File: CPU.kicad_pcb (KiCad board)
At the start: 4 copper layers, 364 x 203 mm, 219 parts, among them J1 Conn_02x36_Top_Bottom, P10 Conn_02x08_Counter_Clockwise, P2 Conn_02x13_Top_Bottom, P3 Conn_02x13_Top_Bottom, P4 Conn_02x08_Counter_Clockwise, P5 Conn_02x25_Counter_Clockwise, P6 Conn_02x25_Counter_Clockwise, P7 Conn_02x07_Counter_Clockwise, P8 Conn_02x08_Counter_Clockwise

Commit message: Second row completed
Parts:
- moved U_B10 0.51 mm to (339.9, 148.4)
- moved U_B9 0.51 mm to (339.9, 135.2)
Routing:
- net Net-(JP1-Pad3): track 16.0 -> 108.8 mm, vias 0 -> 1
- net /Sys.Reset: track 59.1 -> 130.5 mm
- net Net-(U_B7-Pad1): track 0.00 -> 70.3 mm, vias 0 -> 1
- net Net-(U_A15-Pad9): track 0.00 -> 60.9 mm, vias 0 -> 1
- net Address.A_{15}: track 66.0 -> 110.3 mm
- net Net-(U_B6-Pad15): track 0.00 -> 42.8 mm
- net /PTR.Q_{6}: track 96.1 -> 126.6 mm, vias 1 -> 2
- net /~{H14_OE}: track 79.8 -> 105.5 mm
- net /PTR.Q_{5}: track 173.2 -> 182.6 mm
- net /J13_12: track 44.6 -> 51.2 mm
- net Address.A_{12}: track 179.3 -> 173.6 mm
- net Address.A_{14}: track 172.5 -> 166.9 mm
- net Address.A_{13}: track 178.0 -> 174.4 mm
- net Res.D_{3}: track 147.8 -> 144.2 mm
- net /~{AddrHToSys}: track 171.4 -> 168.9 mm
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
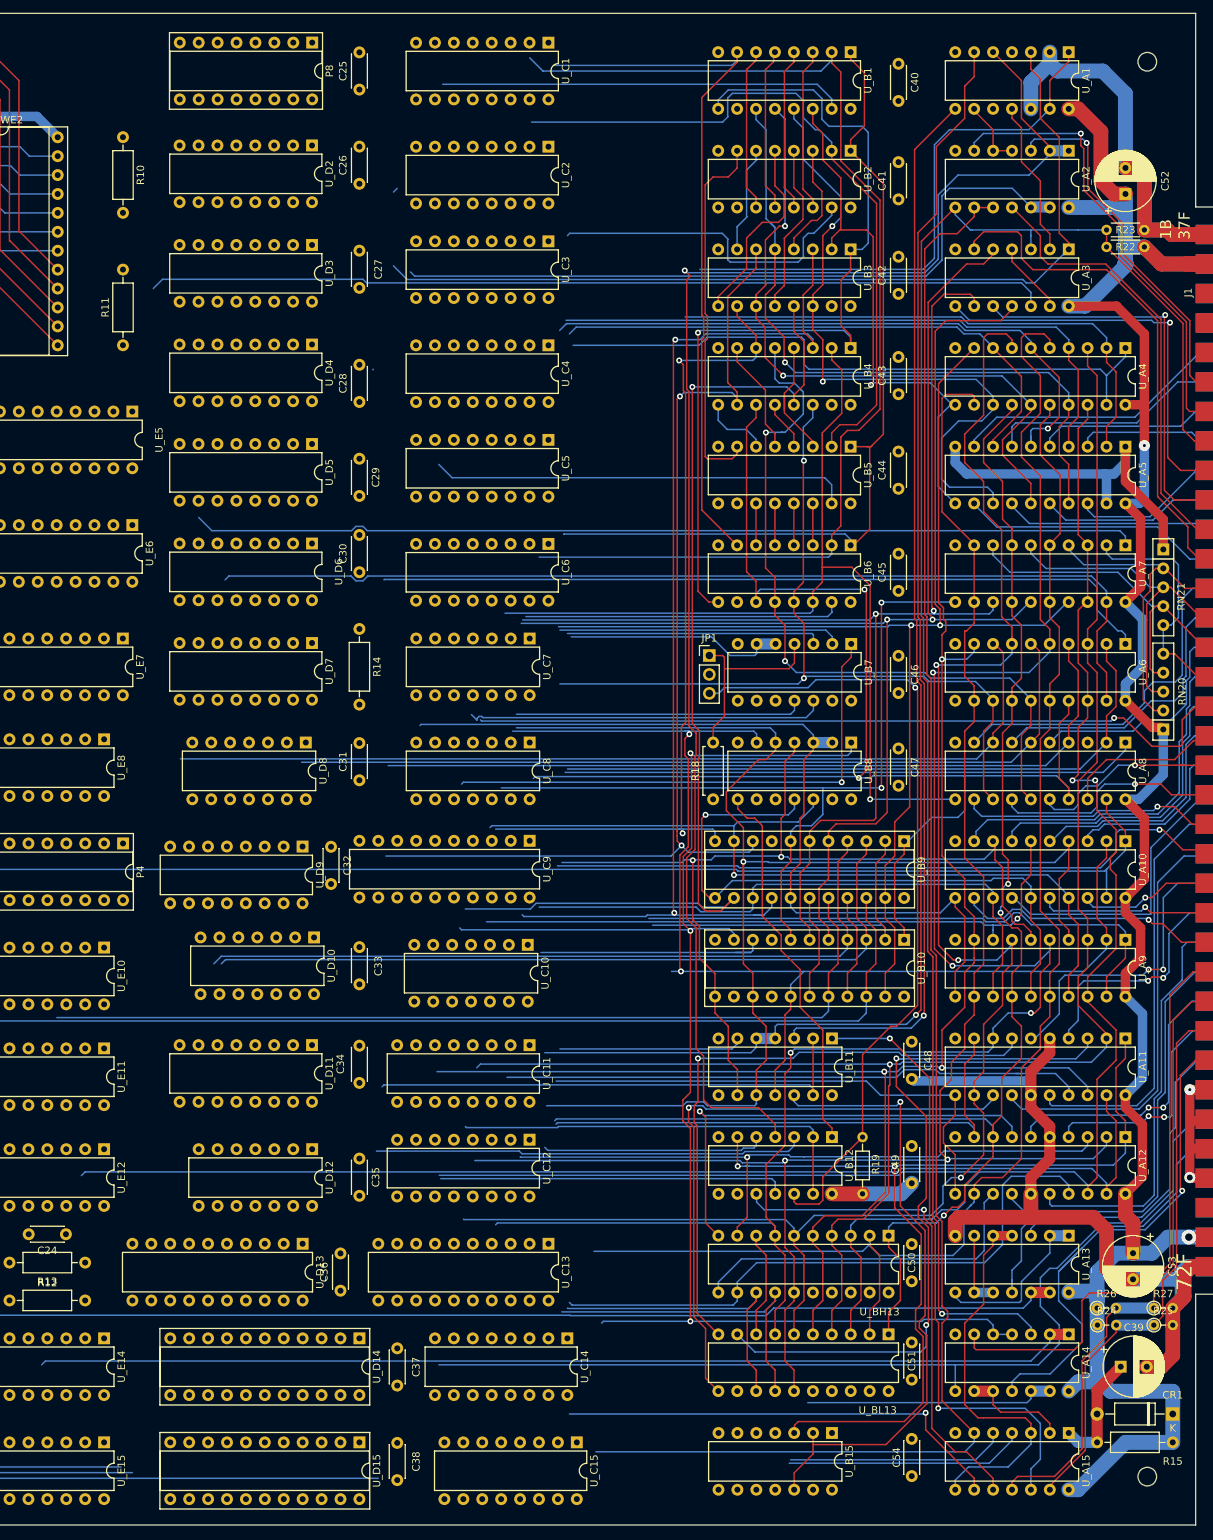
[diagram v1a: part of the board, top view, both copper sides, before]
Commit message: Some power connections
Incomplete PoC
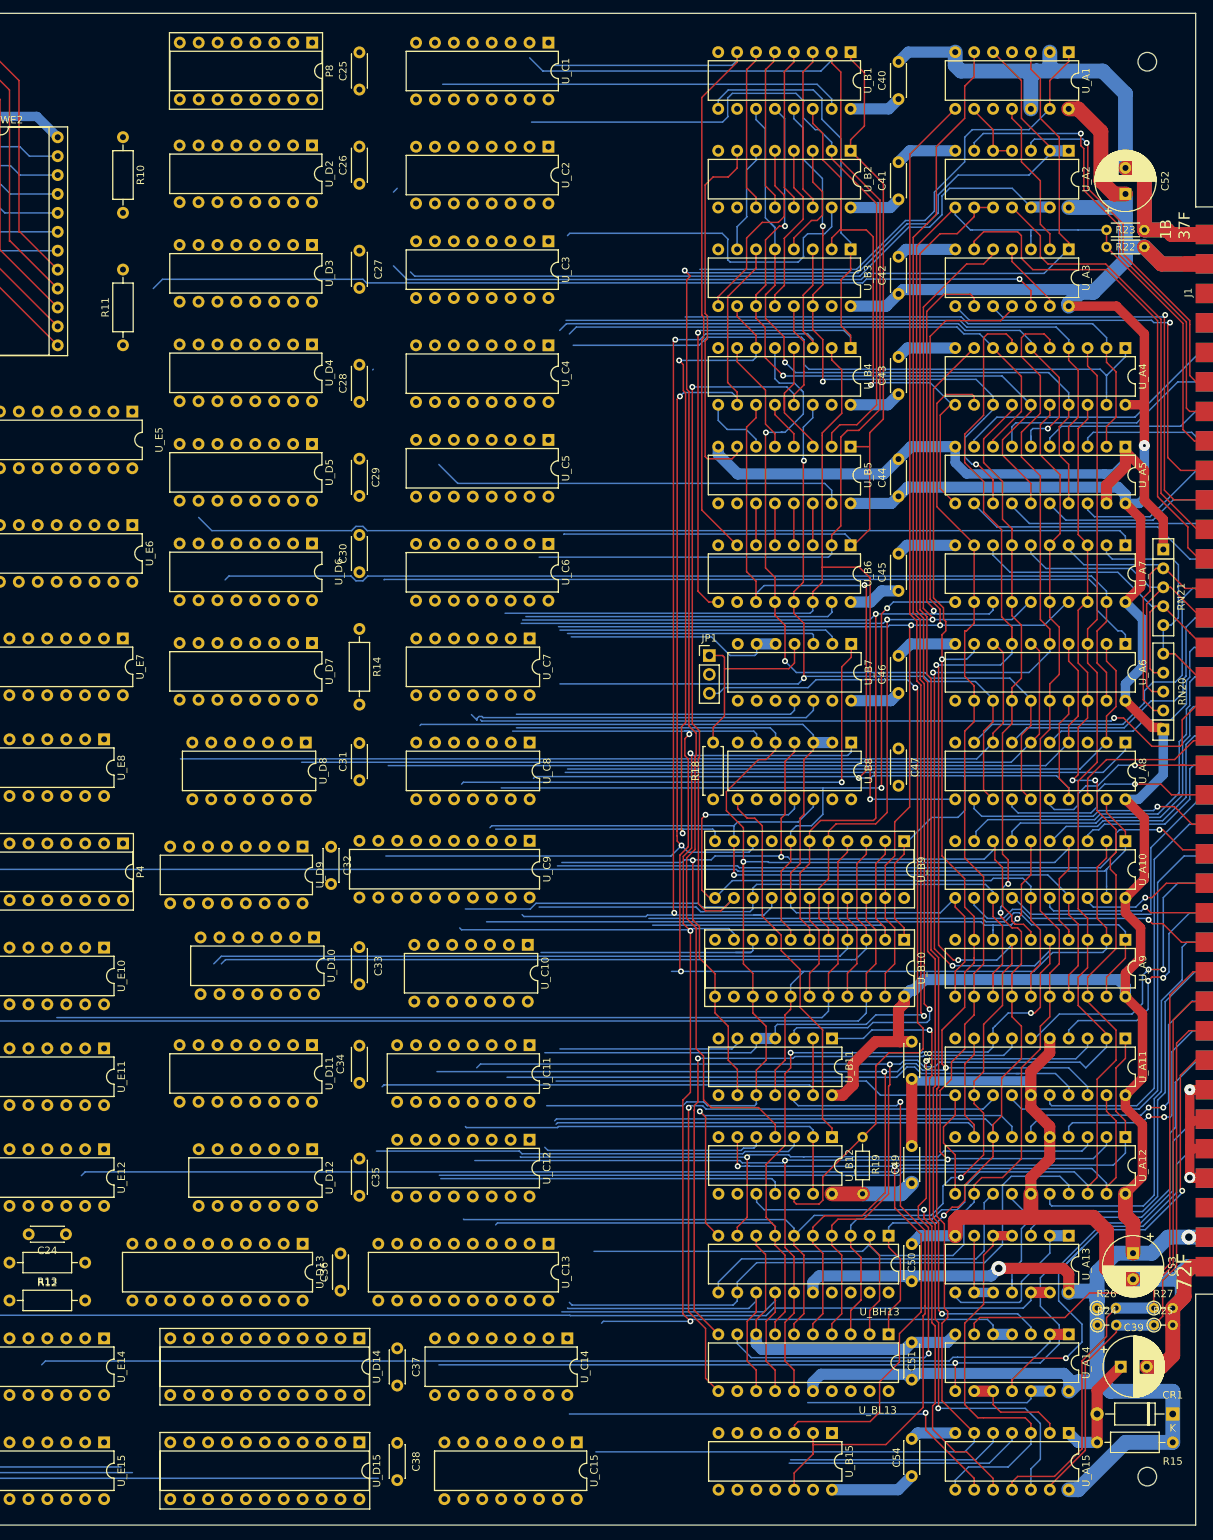
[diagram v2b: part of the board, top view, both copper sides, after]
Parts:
- moved C46 5.00 mm to (339.1, 115.3), turned to 90 degrees
- moved C40 4.75 mm to (339.1, 35.5), turned to 90 degrees
- moved C44 1.02 mm to (339.1, 88.9)
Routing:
- net +5V: track 748.0 -> 999.3 mm, vias 2 -> 3
- net GND: track 1060.8 -> 1212.4 mm
- net Address.A_{1}: track 91.6 -> 82.7 mm, vias 2 -> 3
- net /~{Reset_{2}}: track 73.5 -> 68.0 mm
- net /MemAddr_LD_SWAP: track 118.2 -> 112.7 mm
- net /Sys.~{PTR7_oc}: track 79.3 -> 74.2 mm
- net Net-(U_A15-Pad12): track 84.2 -> 89.1 mm
- net DataF.D_{3}: track 96.0 -> 91.3 mm
- net /DataRDCycle: track 206.3 -> 202.7 mm
- net Net-(U_A2-Pad12): track 97.8 -> 94.2 mm
- net /~{DataRDLatch}: track 126.7 -> 123.2 mm
- net Net-(JP1-Pad3): track 108.8 -> 111.4 mm
- net /~{DataRDCycle}: track 152.2 -> 154.1 mm
- net /~{DataWTCycle}: track 178.1 -> 179.8 mm
- net DataP.D_{3}: track 251.4 -> 252.7 mm
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
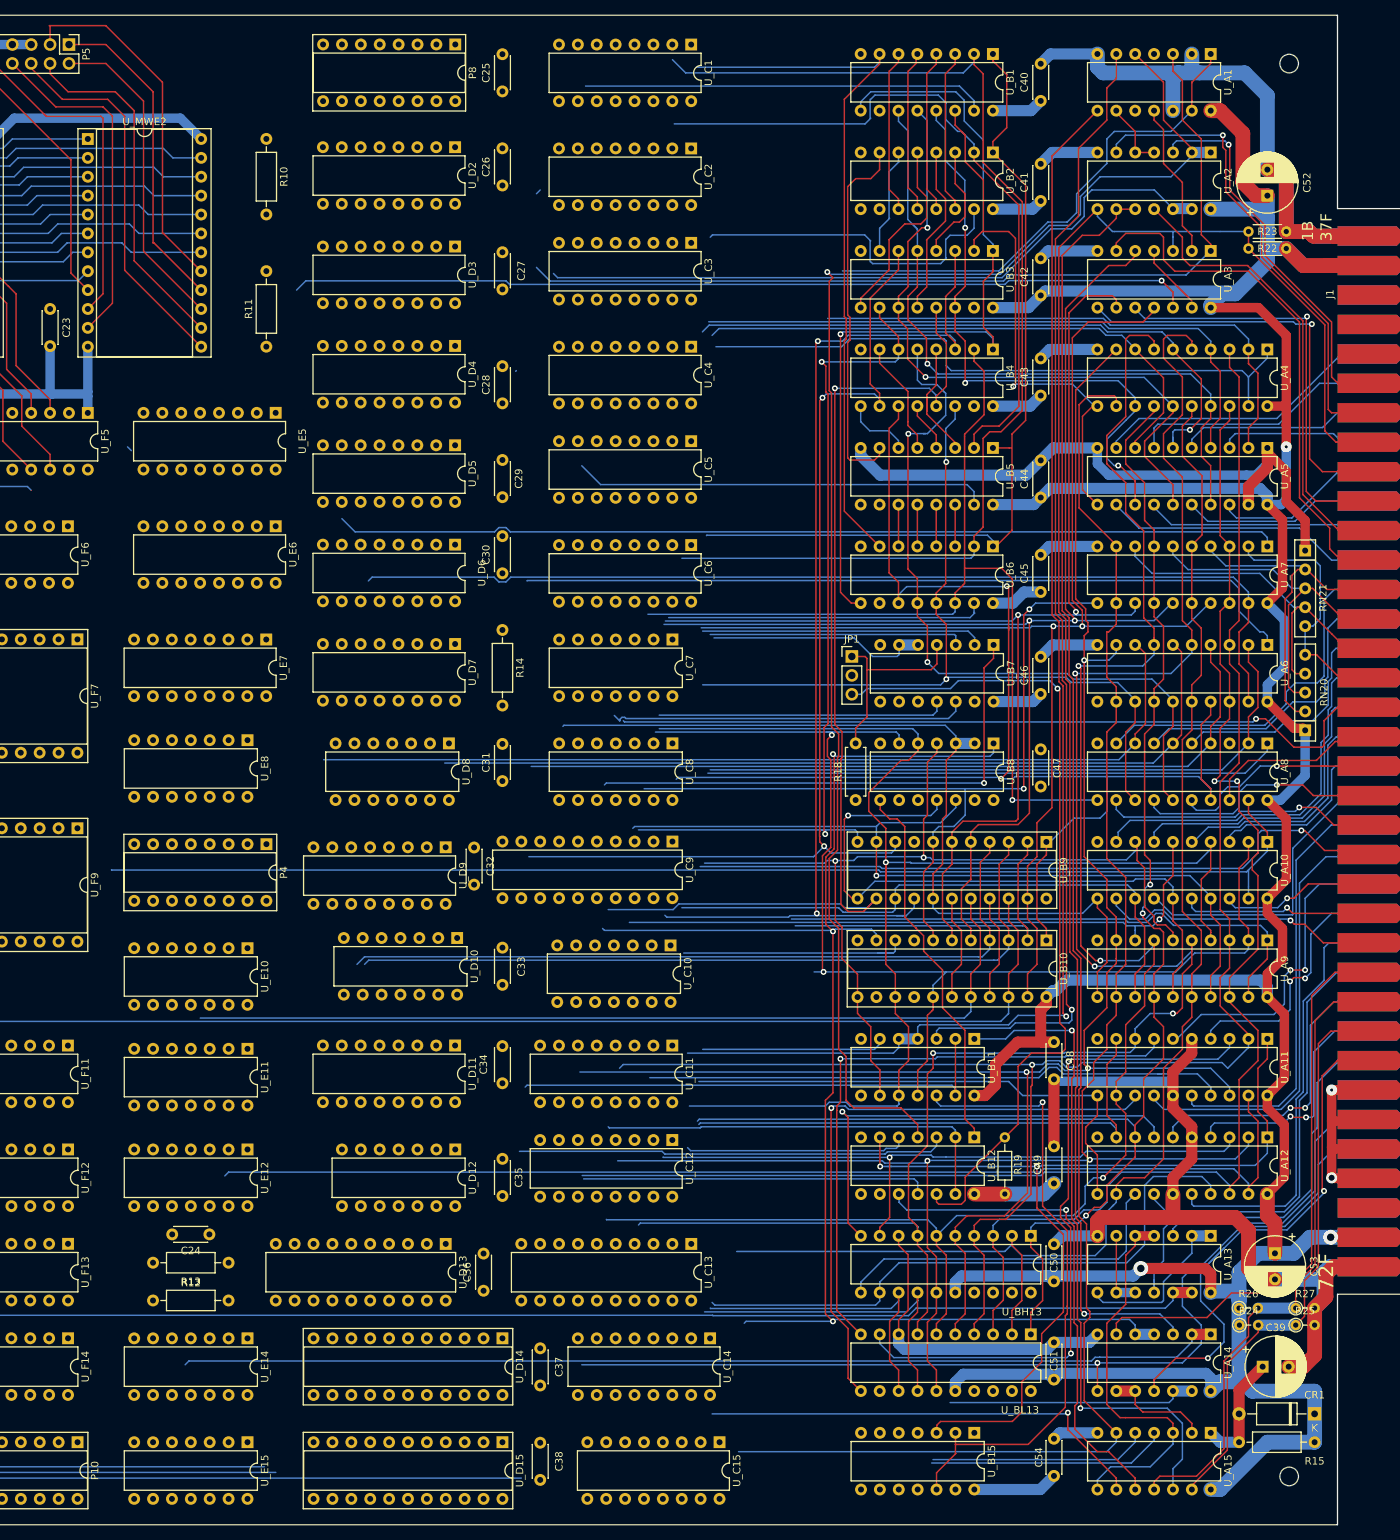
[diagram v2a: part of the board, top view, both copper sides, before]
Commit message: More layout
3rd row ~75% completed
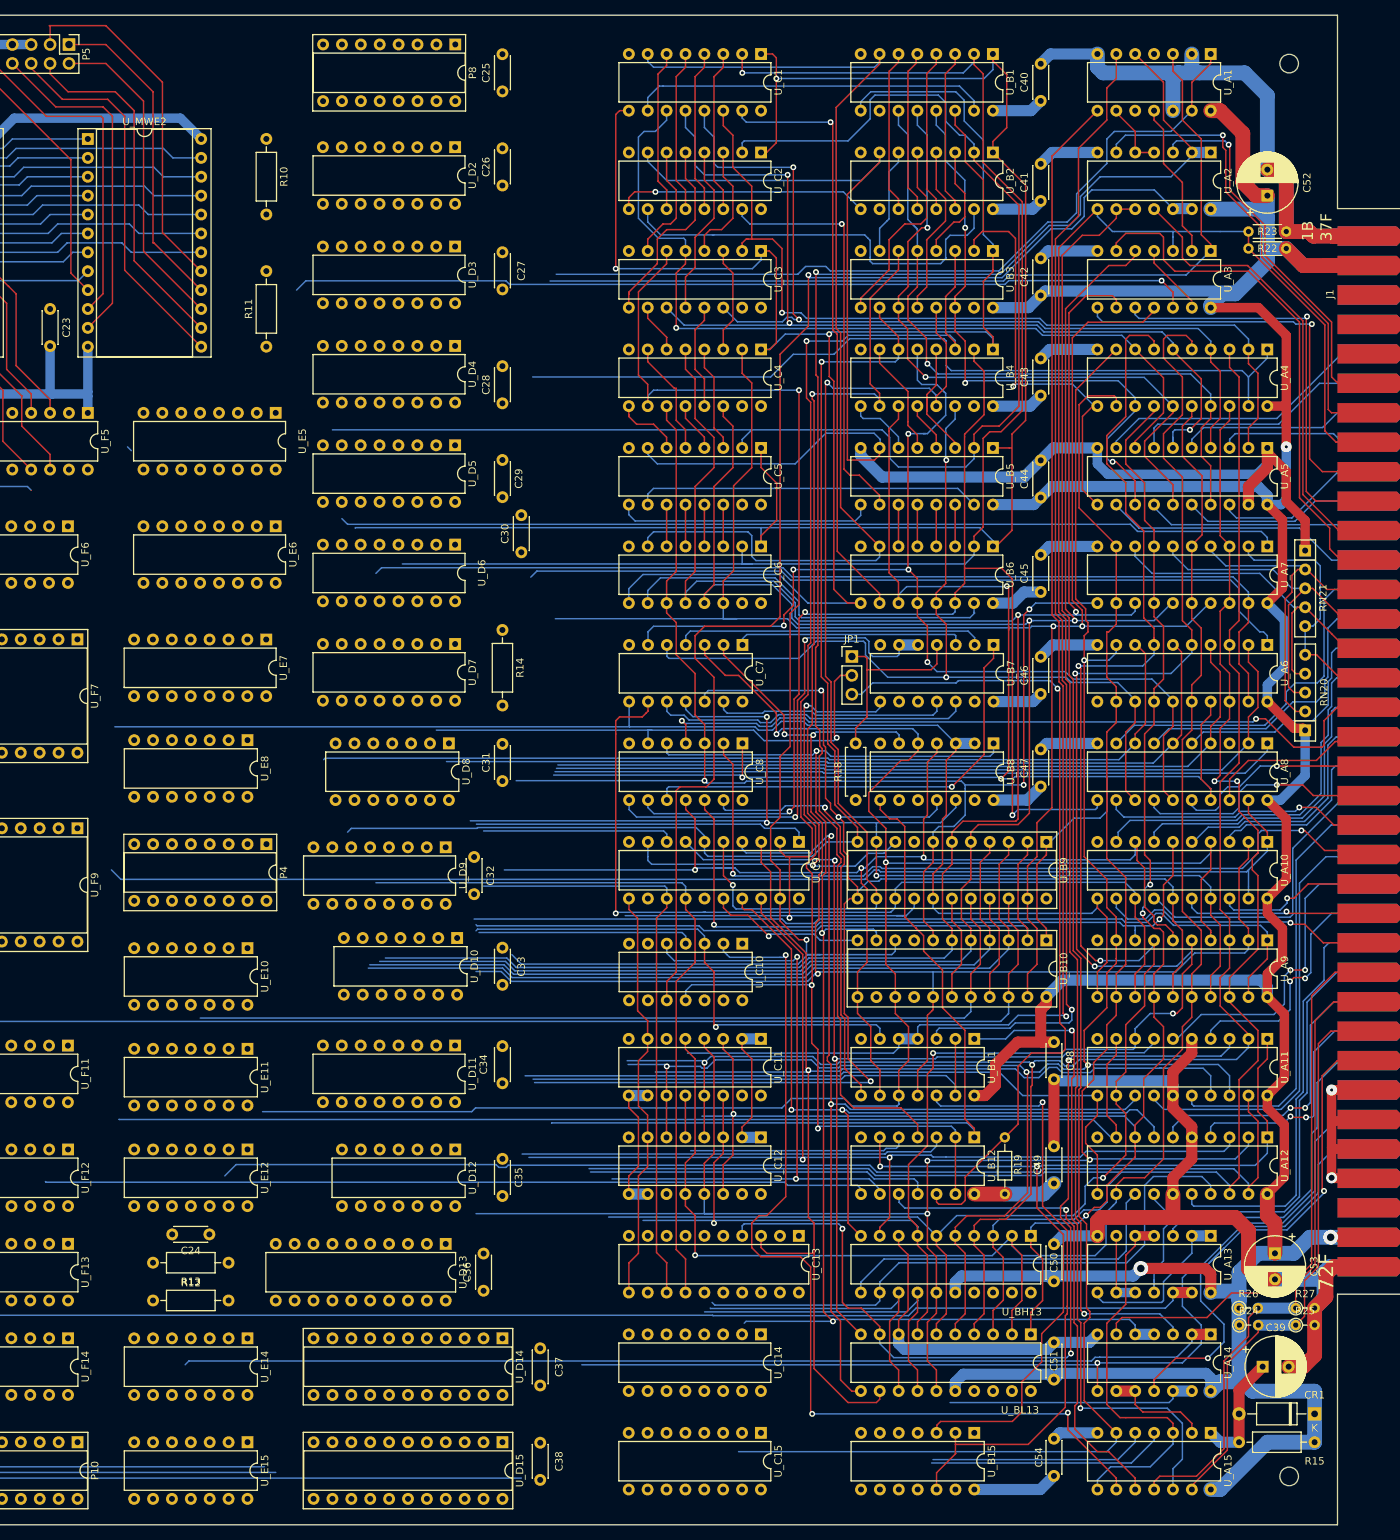
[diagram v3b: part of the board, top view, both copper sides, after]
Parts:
- moved U_C9 17.0 mm to (306.6, 135.2)
- moved U_C13 14.5 mm to (306.6, 188.2)
- moved U_C11 12.0 mm to (301.5, 161.7)
- moved U_C12 11.9 mm to (301.5, 174.9)
- moved U_C10 9.65 mm to (299.0, 148.9)
- moved U_C1 9.48 mm to (301.5, 29.2)
- moved U_C3 9.46 mm to (301.5, 55.7)
- moved U_C7 9.44 mm to (299.0, 108.7)
- moved U_C5 9.44 mm to (301.5, 82.2)
- moved U_C8 9.41 mm to (299.0, 121.9)
- moved U_C2 9.41 mm to (301.5, 42.5)
- moved U_C4 9.40 mm to (301.5, 68.9)
- moved U_C6 9.39 mm to (301.5, 95.4)
- moved U_C14 6.86 mm to (301.5, 201.4)
- moved U_C15 5.71 mm to (301.5, 214.6)
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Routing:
- net Res.D_{7}: track 32.0 -> 181.1 mm, vias 0 -> 2
- net Address.A_{14}: track 167.5 -> 286.5 mm
- net /Addr U/D: track 113.7 -> 228.1 mm, vias 0 -> 1
- net Net-(U_B12-Pad8): track 0.00 -> 110.8 mm
- net Address.A_{13}: track 174.9 -> 285.7 mm
- net /PTR.Q_{2}: track 85.7 -> 195.4 mm, vias 1 -> 3
- net /MemAddr_LD_SWAP: track 112.7 -> 220.9 mm, vias 1 -> 2
- net DataF.D_{5}: track 47.0 -> 145.6 mm
- net DataF.D_{0}: track 78.7 -> 175.1 mm, vias 0 -> 1
- net Net-(U_B2-Pad2): track 94.7 -> 182.9 mm
- net /INT_ENABLE: track 0.00 -> 86.6 mm, vias 0 -> 2
- net Net-(U_B6-Pad10): track 0.00 -> 80.6 mm, vias 0 -> 1
- net DataF.D_{4}: track 83.5 -> 163.8 mm
- net Net-(U_A2-Pad12): track 94.2 -> 174.1 mm, vias 0 -> 1
- net /~{DataWT_EN}: track 72.9 -> 149.9 mm
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
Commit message: Third row of chips completed
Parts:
- moved U_D13 9.72 mm to (268.7, 188.2)
- moved C36 9.24 mm to (273.1, 193.0)
- moved C26 6.69 mm to (273.3, 48.0)
- moved C25 6.35 mm to (272.8, 36.0)
- moved C32 6.25 mm to (267.0, 141.9), turned to 90 degrees
- moved C30 5.92 mm to (272.3, 101.3)
- moved C33 5.90 mm to (265.4, 155.2), turned to 90 degrees
- moved C27 5.69 mm to (272.3, 56.9)
- moved C28 5.64 mm to (272.3, 75.4)
- moved C29 5.62 mm to (272.3, 84.4)
- moved U_C14 5.10 mm to (306.6, 201.4)
- moved U_C15 5.10 mm to (306.6, 214.6)
- moved C35 4.90 mm to (265.7, 182.6), turned to 90 degrees
- moved U_D15 4.80 mm to (271.3, 214.6)
- moved U_D14 4.66 mm to (271.3, 201.4)
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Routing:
- net Res.D_{4}: track 14.3 -> 355.7 mm, vias 0 -> 3
- net Res.D_{5}: track 14.3 -> 348.4 mm, vias 0 -> 4
- net /INT_ACK: track 33.8 -> 292.2 mm
- net /DMAAddressControl: track 0.00 -> 211.7 mm, vias 0 -> 1
- net /CondMemFault: track 0.00 -> 193.0 mm
- net Res.D_{6}: track 28.0 -> 187.4 mm, vias 1 -> 3
- net /Sys.Reset: track 131.0 -> 261.4 mm, vias 1 -> 2
- net /CPL_{3}: track 124.8 -> 231.1 mm, vias 0 -> 2
- net MW.A6_{7}: track 10.0 -> 115.5 mm
- net /~{Swap_OE}: track 19.4 -> 124.2 mm, vias 0 -> 1
- net /CPL_{0}: track 109.1 -> 210.9 mm, vias 0 -> 2
- net /PTR.Q_{7}: track 191.1 -> 288.3 mm
- net /CPL_{2}: track 113.3 -> 209.6 mm, vias 0 -> 2
- net Net-(U_C10-Pad13): track 0.00 -> 95.3 mm, vias 0 -> 2
- net /CPL_{1}: track 103.7 -> 197.4 mm, vias 0 -> 2
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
